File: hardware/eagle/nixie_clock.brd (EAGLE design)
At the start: 213.4 x 168.9 mm, 67 parts, among them IC1 74141N, IC10 7477N, IC11 74141N, IC12 7477N, IC13 74AC11238, IC2 7477N, IC3 74141N, IC4 7477N, IC5 74141N, IC6 7477N, IC7 74141N, IC8 7477N, IC9 74141N, J1_180V 22-27-2021-02, J1_5V1 22-27-2021-02, J1_5V2 22-27-2021-02, K1 4052, SW1 ROTARTY_ENCODER

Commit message: Working on Sunday
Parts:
- removed Q1: (no value), SparkFun-DiscreteSemi:TO-92
- added C16: 100nF, resistor:C025-024X044
- added D1: LED-RGB-CA-THRUCLEAR, SparkFun-LED:LED-RGB-THRU
- added ULN1: (no value), SparkFun-PowerIC:DIL18
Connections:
- removed net N$124: C1.2, C10.2, C11.2, C12.2, C13.2, C2.2, C3.2, C4.2, C5.2, C6.2, C7.2, C8.2, C9.2, IC1.5, IC10.4, IC11.5, IC12.4, IC13.11, IC13.12, IC2.4, IC3.5, IC4.4, IC5.5, IC6.4, IC7.5, IC8.4, IC9.5, J1_5V1.2, Q1.3
- new net N$138: GPIO_HEADER1.8, ULN1.2
- new net N$139: GPIO_HEADER1.10, ULN1.3
- new net N$140: C1.2, C10.2, C11.2, C12.2, C13.2, C16.2, C2.2, C3.2, C4.2, C5.2, C6.2, C7.2, C8.2, C9.2, IC1.5, IC10.4, IC11.5, IC12.4, IC13.11, IC13.12, IC2.4, IC3.5, IC4.4, IC5.5, IC6.4, IC7.5, IC8.4, IC9.5, J1_5V1.2, ULN1.10
- net GND: now also C16.1, ULN1.9
- net N$137: now also ULN1.1; no longer Q1.2

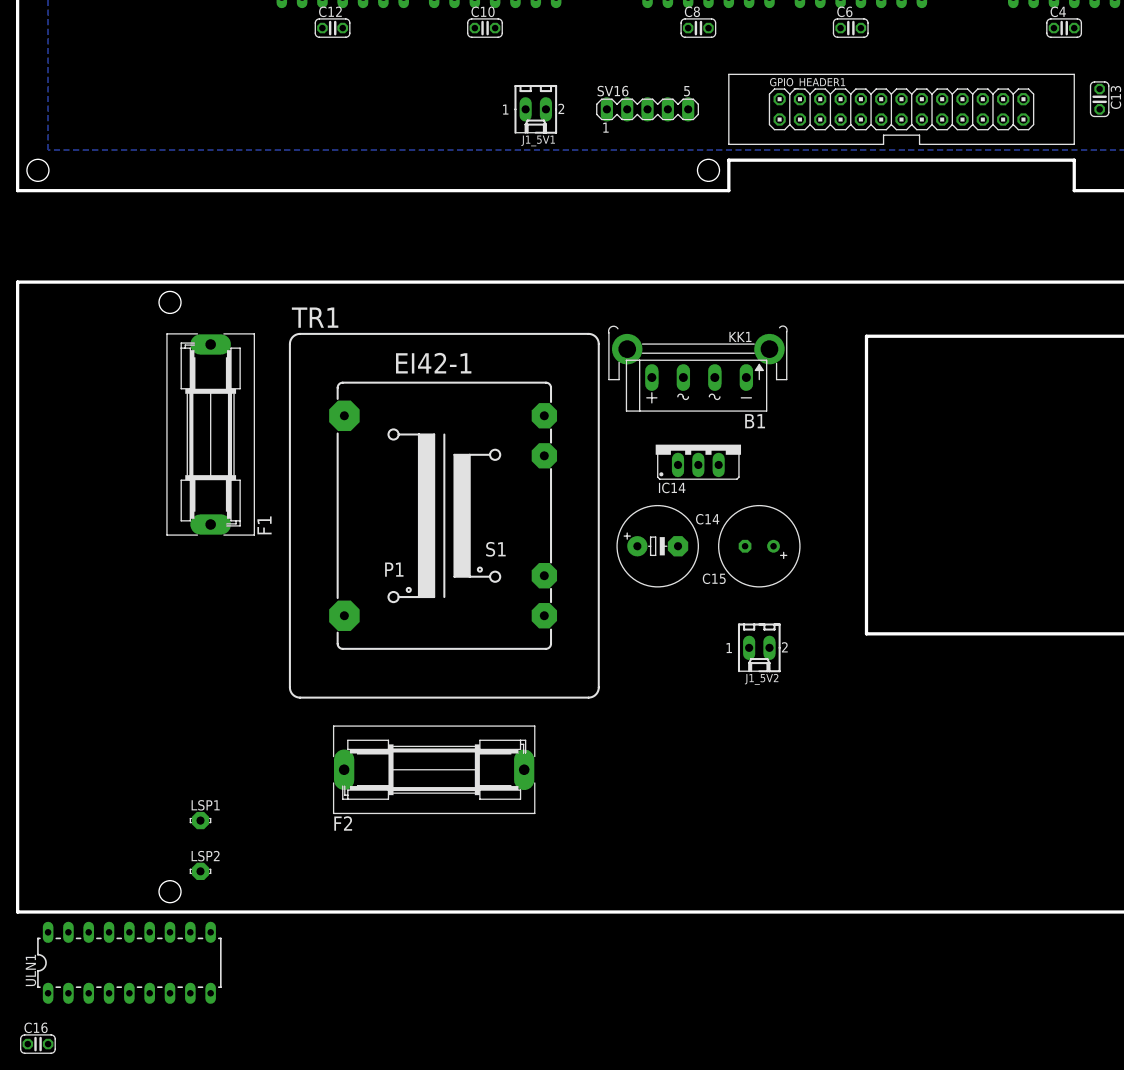
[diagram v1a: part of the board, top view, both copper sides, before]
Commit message: Added uln documentation
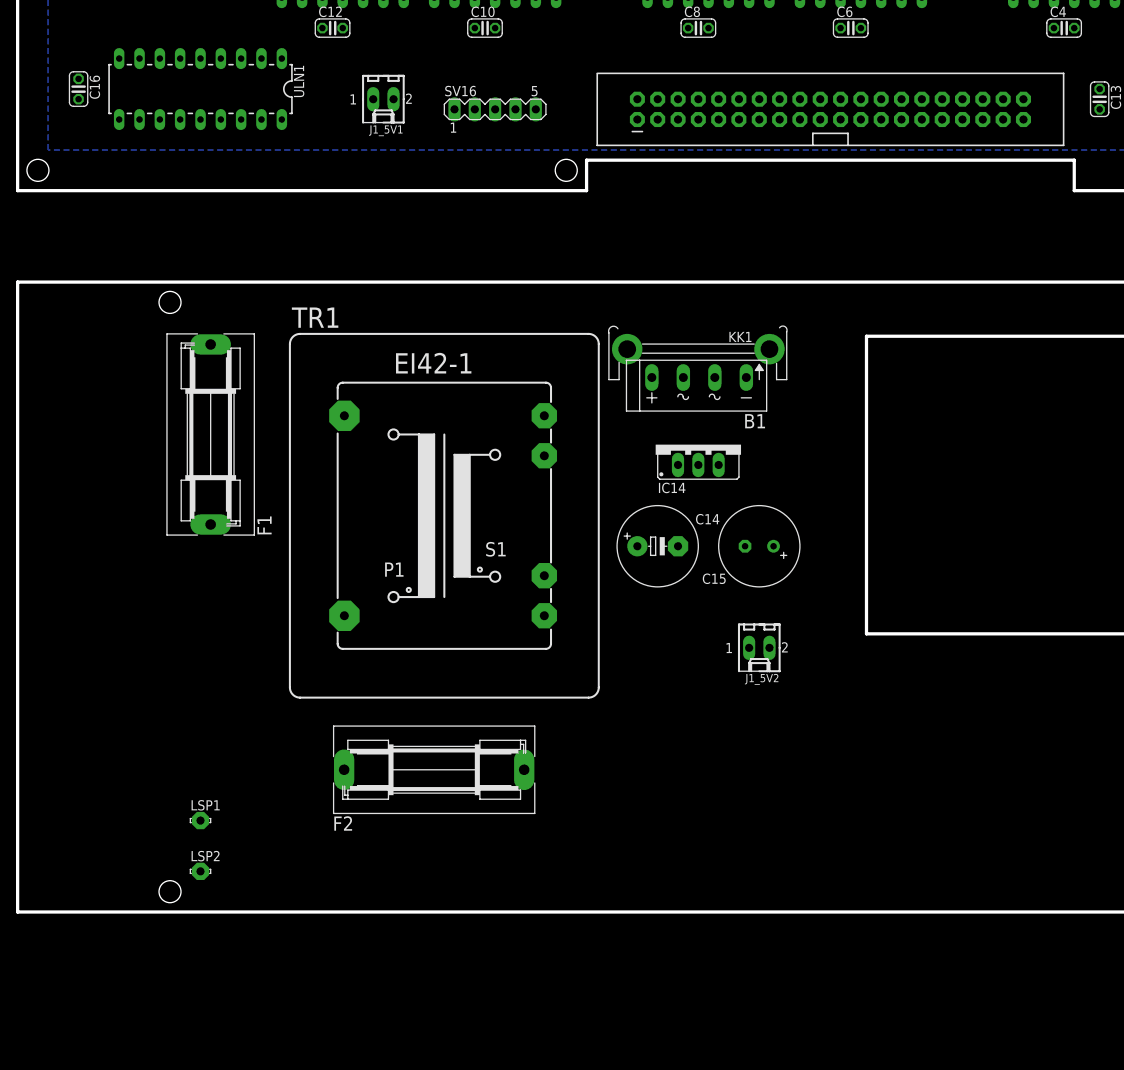
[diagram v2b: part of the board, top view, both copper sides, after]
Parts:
- removed GPIO_HEADER1: RPI_GPIO_HEADER, rpi-header:2X13
- added J1: RASPBERRYPI-40-PIN-GPIO, SparkFun-Boards:2X20-SHROUDED
- moved C16 119.5 mm to (7.62, 12.7), turned to 270 degrees
- moved ULN1 109.6 mm to (22.9, 12.7), turned to 180 degrees
- moved J1_5V1 19.1 mm to (45.7, 11.4)
- moved SV16 19.0 mm to (59.7, 10.2)
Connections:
- removed net +3V3: GPIO_HEADER1.1, GPIO_HEADER1.17
- removed net +5V: GPIO_HEADER1.2, GPIO_HEADER1.4
- removed net N$135: GPIO_HEADER1.26, SV16.5
- removed net N$136: GPIO_HEADER1.21, SV16.3
- new net 3.3V: J1.1, J1.17
- new net 5V: J1.2, J1.4
- new net N$124: J1.26, SV16.5
- net GND: now also J1.14, J1.20, J1.25, J1.30, J1.34, J1.39, J1.6, J1.9; no longer GPIO_HEADER1.14, GPIO_HEADER1.20, GPIO_HEADER1.25, GPIO_HEADER1.6, GPIO_HEADER1.9
- net N$127: now also J1.19; no longer GPIO_HEADER1.19
- net N$129: now also J1.7; no longer GPIO_HEADER1.7
- net N$130: now also J1.21, SV16.3; no longer GPIO_HEADER1.24
- net N$137: now also J1.23; no longer GPIO_HEADER1.23
- net N$138: now also J1.8; no longer GPIO_HEADER1.8
- net N$139: now also J1.10; no longer GPIO_HEADER1.10
- net N$17: now also J1.15; no longer GPIO_HEADER1.15
- net N$94: now also J1.16; no longer GPIO_HEADER1.16
- net N$95: now also J1.18; no longer GPIO_HEADER1.18
- net N$96: now also J1.22; no longer GPIO_HEADER1.22
- net N$97: now also J1.13; no longer GPIO_HEADER1.13
- net N$98: now also J1.12; no longer GPIO_HEADER1.12
- net N$99: now also J1.11; no longer GPIO_HEADER1.11
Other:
- outline, holes or cut-outs redrawn

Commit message: Updated project
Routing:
- net N$140: track 0.00 -> 369.4 mm, vias 0 -> 4
- net N$17: track 0.00 -> 210.0 mm, vias 0 -> 7
- net N$94: track 0.00 -> 164.8 mm, vias 0 -> 4
- net N$95: track 0.00 -> 158.4 mm, vias 0 -> 2
- net VCC: track 0.00 -> 147.0 mm
- net N$99: track 0.00 -> 144.1 mm, vias 0 -> 1
- net N$96: track 0.00 -> 142.6 mm, vias 0 -> 3
- net N$93: track 0.00 -> 135.3 mm, vias 0 -> 5
- net N$130: track 0.00 -> 129.3 mm, vias 0 -> 2
- net N$129: track 0.00 -> 126.8 mm, vias 0 -> 1
- net N$78: track 0.00 -> 126.4 mm, vias 0 -> 2
- net N$137: track 0.00 -> 125.1 mm, vias 0 -> 4
- net N$63: track 0.00 -> 87.9 mm, vias 0 -> 5
- net N$98: track 0.00 -> 69.9 mm, vias 0 -> 1
- net N$48: track 0.00 -> 68.3 mm, vias 0 -> 3
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
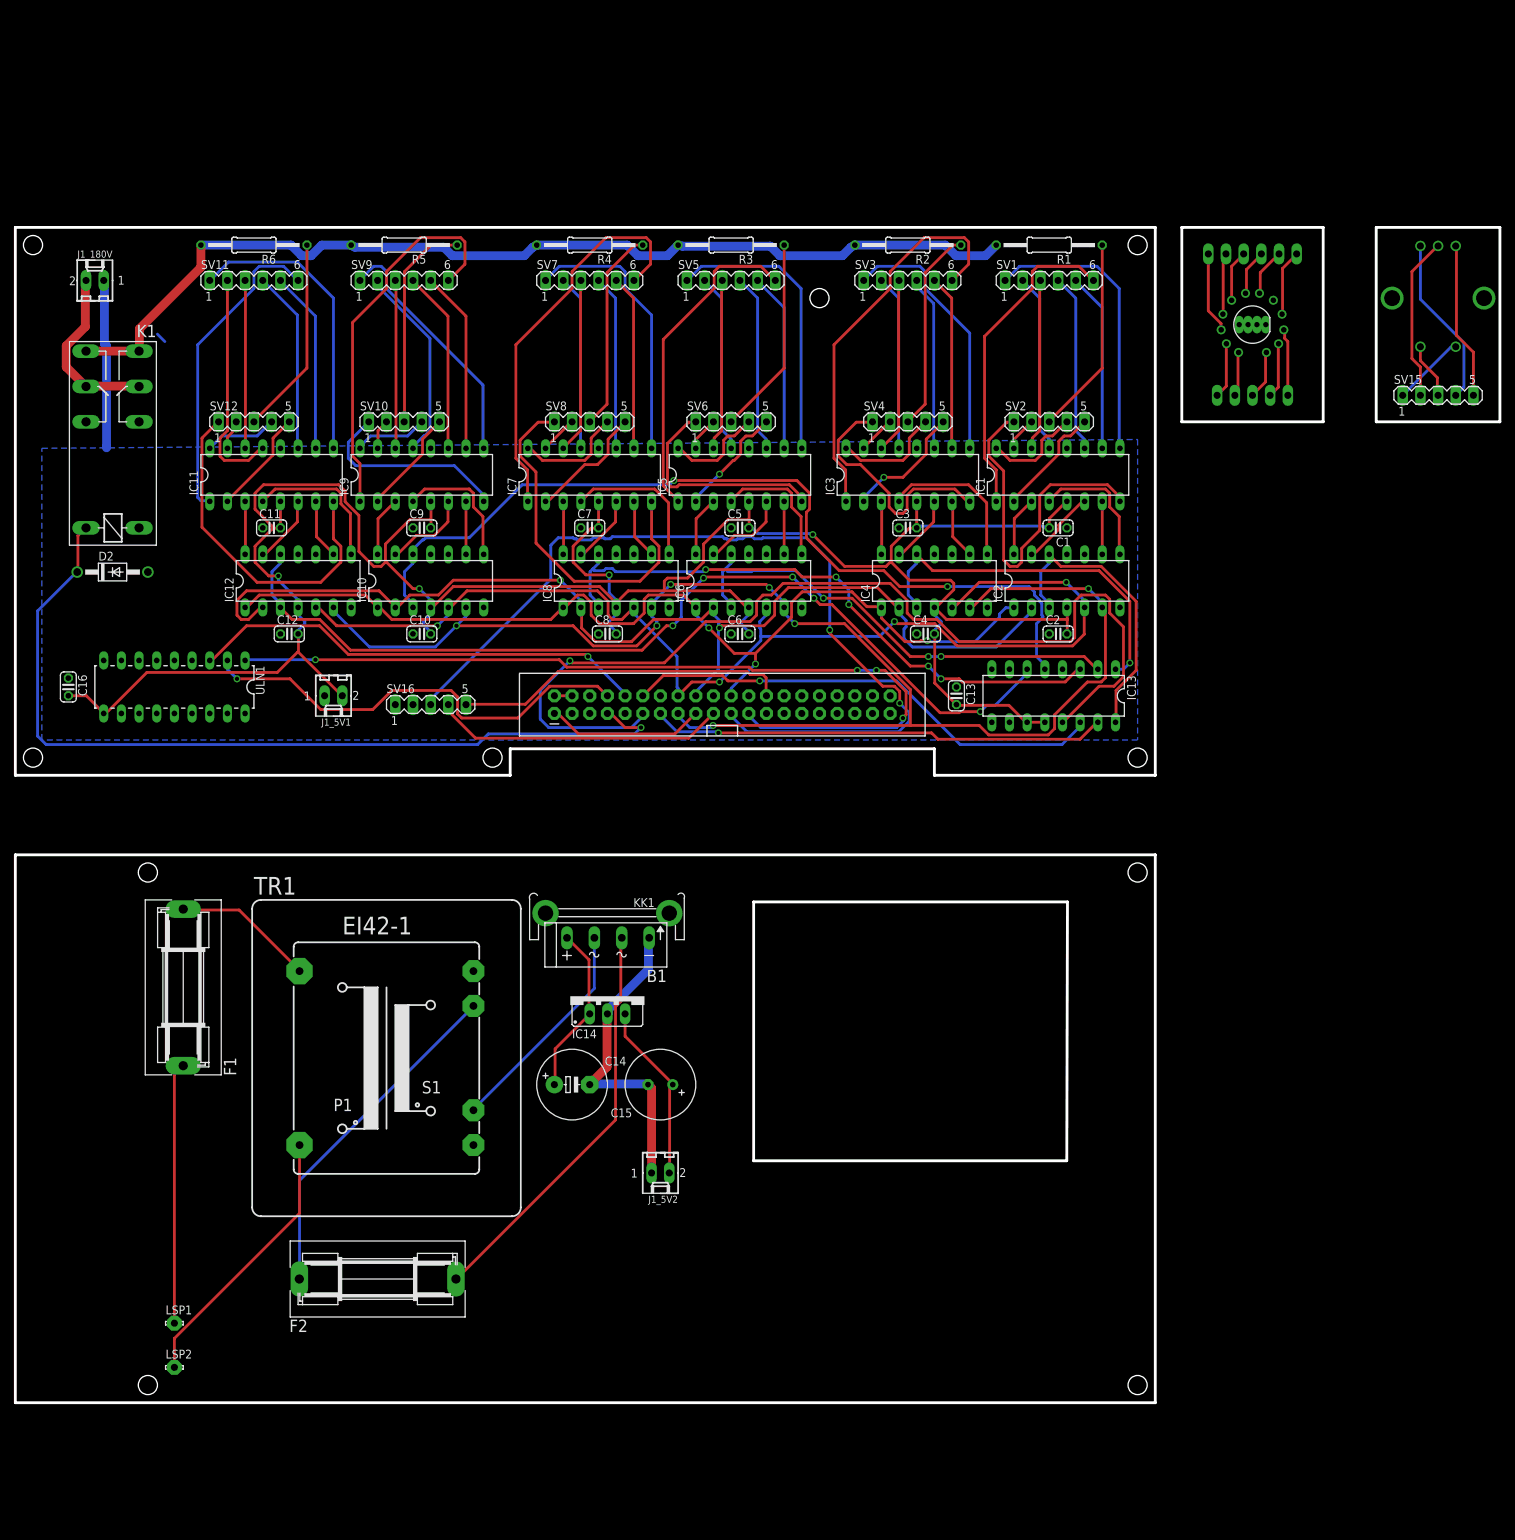
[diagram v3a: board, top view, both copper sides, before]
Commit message: Added new model on freecad model and updated pcb board
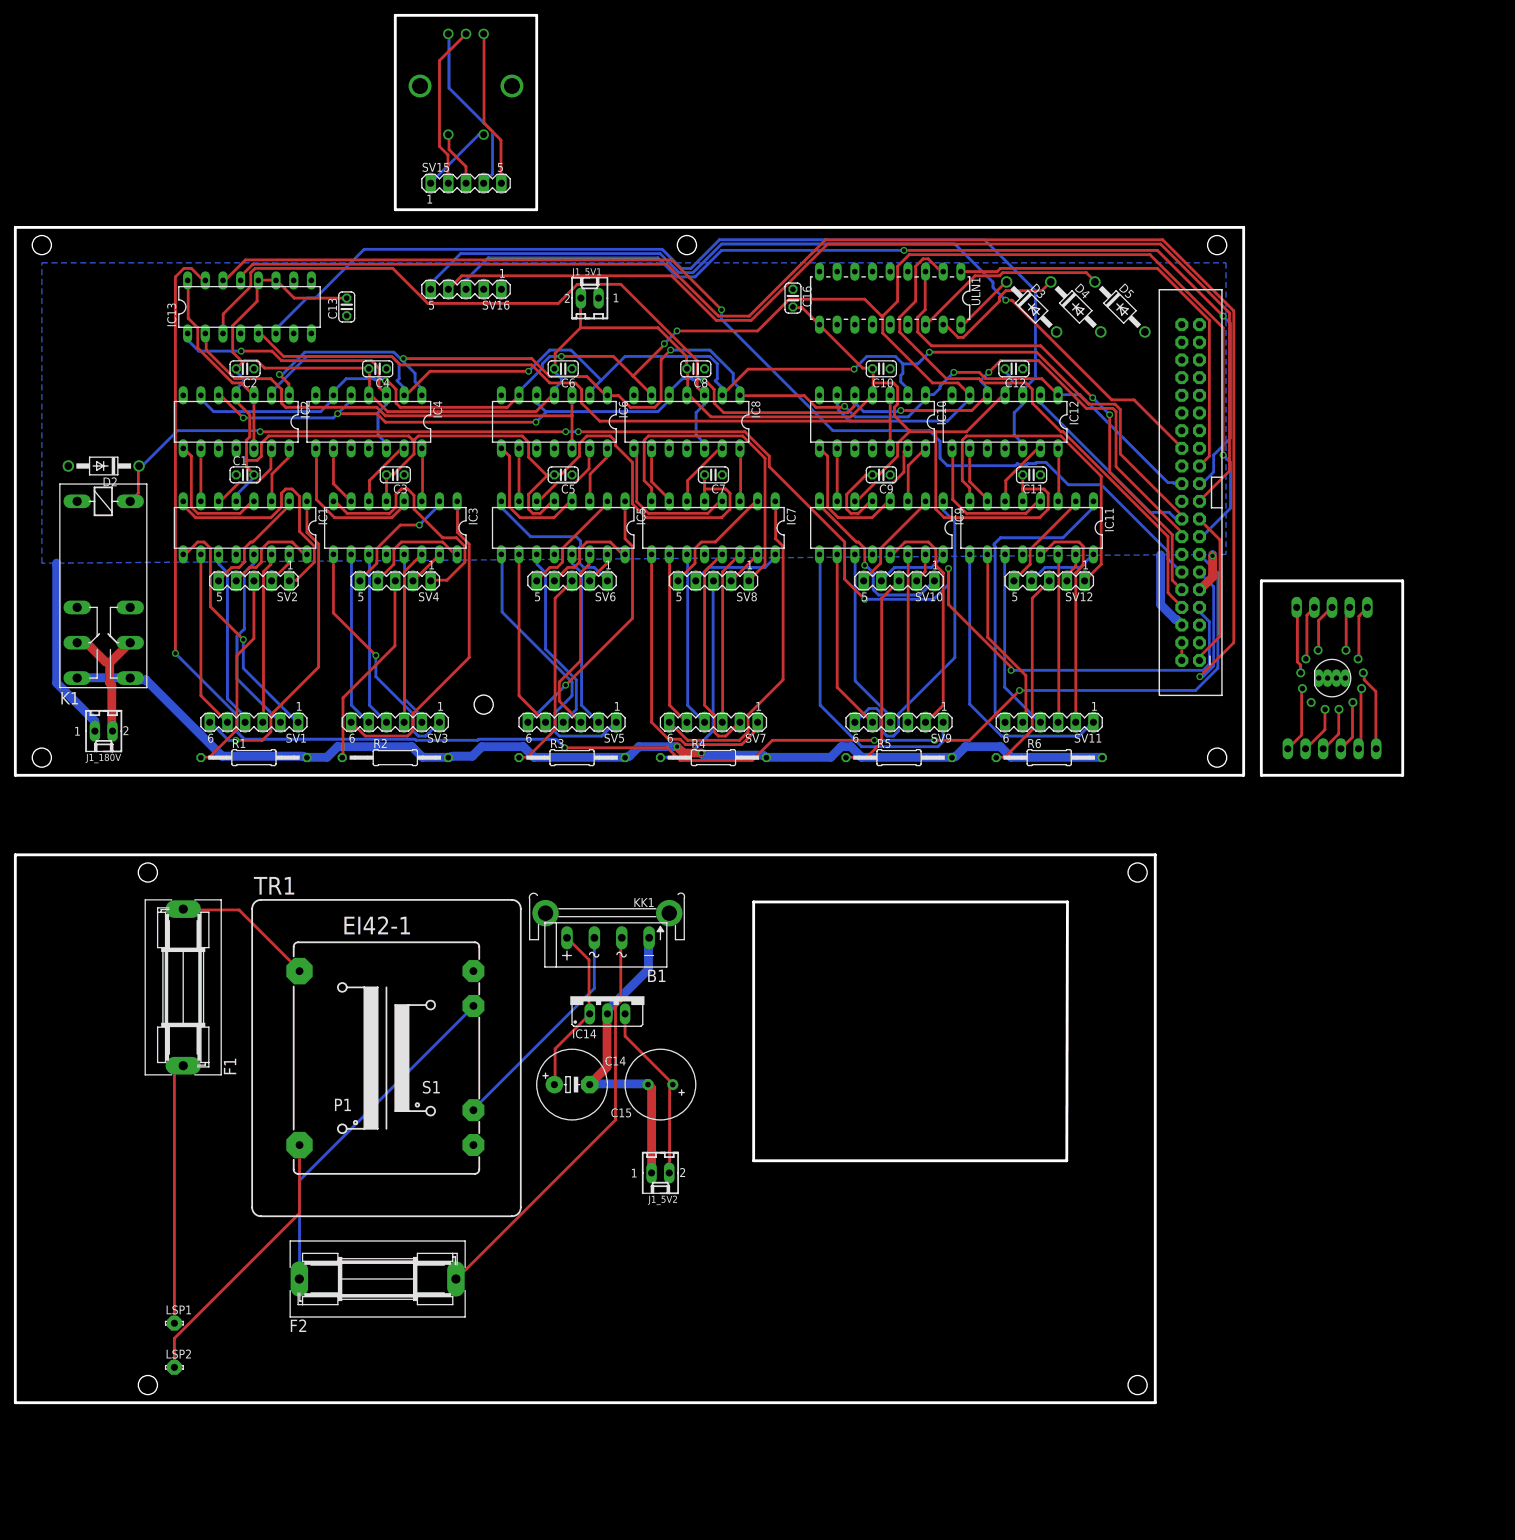
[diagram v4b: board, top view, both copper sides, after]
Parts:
- added D3, D4, D5: 1N4004, diode:DO41-10
- moved SV15 143.0 mm to (64.8, 85.1)
- moved SW1 143.0 mm to (64.8, 99.1)
- moved R1 136.0 mm to (34.3, 2.54), turned to 0 degrees
- moved R6 136.0 mm to (148.6, 2.54), turned to 0 degrees
- moved SV1 130.8 mm to (34.3, 7.62), turned to 180 degrees
- moved SV11 130.8 mm to (148.6, 7.62), turned to 180 degrees
- moved IC13 128.4 mm to (33.7, 67.3), turned to 0 degrees
- moved C2 122.9 mm to (33.0, 58.4), turned to 180 degrees
- moved IC2 121.5 mm to (31.8, 50.8), turned to 180 degrees
- moved C16 118.2 mm to (111.8, 68.6)
- moved C1 117.1 mm to (33.0, 43.2), turned to 0 degrees
- moved IC1 117.1 mm to (33.0, 35.6), turned to 180 degrees
- moved ULN1 117.1 mm to (125.7, 68.6)
- moved SV12 116.6 mm to (148.6, 27.9), turned to 180 degrees
- moved SV2 116.6 mm to (34.3, 27.9), turned to 180 degrees
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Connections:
- new net N$116: D4.C, ULN1.17
- new net N$135: D3.C, ULN1.18
- new net N$136: D5.C, ULN1.16
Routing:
- net N$97: track 65.6 -> 240.3 mm, vias 1 -> 5
- net N$127: track 42.1 -> 153.2 mm
- net N$98: track 69.9 -> 161.1 mm
- net N$99: track 144.1 -> 227.5 mm
- net N$124: track 48.2 -> 126.1 mm, vias 0 -> 1
- net N$129: track 126.8 -> 197.2 mm, vias 1 -> 6
- net N$137: track 125.1 -> 60.5 mm, vias 4 -> 0
- net N$95: track 158.4 -> 202.8 mm, vias 2 -> 3
- net N$17: track 210.0 -> 253.8 mm, vias 7 -> 5
- net N$140: track 369.4 -> 401.2 mm, vias 4 -> 0
- net N$136: track 0.00 -> 28.0 mm
- net N$96: track 142.6 -> 166.5 mm, vias 3 -> 5
- net N$78: track 126.4 -> 104.8 mm, vias 2 -> 0
- net GND: track 24.2 -> 43.7 mm, vias 0 -> 1
- net N$116: track 1.51 -> 19.9 mm
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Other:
- board size 213.4 x 168.9 mm -> 199.4 x 199.4 mm

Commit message: Updated project: new documentation & more ...
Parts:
- removed IC13: 74AC11238, 74ac-logic:DIL16
- added U$1: M74HC238, SparkFun-DigitalIC:DIL16
- moved TR1 14.0 mm to (39.4, -40.6)
- moved B1 14.0 mm to (71.1, -24.1)
- moved C14 14.0 mm to (66.0, -44.5)
- moved C15 14.0 mm to (78.7, -44.5)
- moved F1 14.0 mm to (10.2, -30.5)
- moved F2 14.0 mm to (38.1, -72.4)
- moved IC14 14.0 mm to (71.1, -31.8)
- moved J1_5V2 14.0 mm to (78.7, -57.1)
- moved KK1 14.0 mm to (71.1, -20.3)
- moved LSP1 14.0 mm to (8.89, -78.7)
- moved LSP2 14.0 mm to (8.89, -85.1)
- moved C13 1.91 mm to (49.5, 67.3)
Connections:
- net GND: now also C13.2, U$1.4, U$1.5, U$1.8; no longer C13.1, IC13.10, IC13.4, IC13.9
- net N$140: now also C13.1, U$1.16, U$1.6; no longer C13.2, IC13.11, IC13.12
- net N$16: now also U$1.15; no longer IC13.16
- net N$33: now also U$1.14; no longer IC13.1
- net N$48: now also U$1.13; no longer IC13.2
- net N$63: now also U$1.12; no longer IC13.3
- net N$78: now also U$1.11; no longer IC13.5
- net N$93: now also U$1.10; no longer IC13.6
- net N$97: now also U$1.1; no longer IC13.15
- net N$98: now also U$1.2; no longer IC13.14
- net N$99: now also U$1.3; no longer IC13.13
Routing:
- net N$140: track 401.2 -> 0.00 mm
- net N$17: track 253.8 -> 0.00 mm, vias 5 -> 0
- net N$97: track 240.3 -> 0.00 mm, vias 5 -> 0
- net N$99: track 227.5 -> 0.00 mm, vias 1 -> 0
- net N$95: track 202.8 -> 0.00 mm, vias 3 -> 0
- net N$129: track 197.2 -> 0.00 mm, vias 6 -> 0
- net N$94: track 178.1 -> 0.00 mm, vias 6 -> 0
- net N$96: track 166.5 -> 0.00 mm, vias 5 -> 0
- net N$98: track 161.1 -> 0.00 mm, vias 1 -> 0
- net VCC: track 158.4 -> 0.00 mm, vias 2 -> 0
- net N$127: track 153.2 -> 0.00 mm
- net N$93: track 144.8 -> 0.00 mm
- net N$130: track 144.7 -> 0.00 mm, vias 2 -> 0
- net N$124: track 126.1 -> 0.00 mm, vias 1 -> 0
- net N$78: track 104.8 -> 0.00 mm
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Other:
- outline, holes or cut-outs redrawn
